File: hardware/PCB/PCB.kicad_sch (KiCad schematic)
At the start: 35 parts, among them J1 USB_C_Receptacle_USB2.0_16P, J2 Conn_01x05_Socket, SW1 SW_Push, SW2 SW_Push, SW3 SW_Push, U1 ESP32-S3-WROOM-1, U2 TPD4E02B04DQA, U3 SX1262 Core, U4 TPS63802DLAR

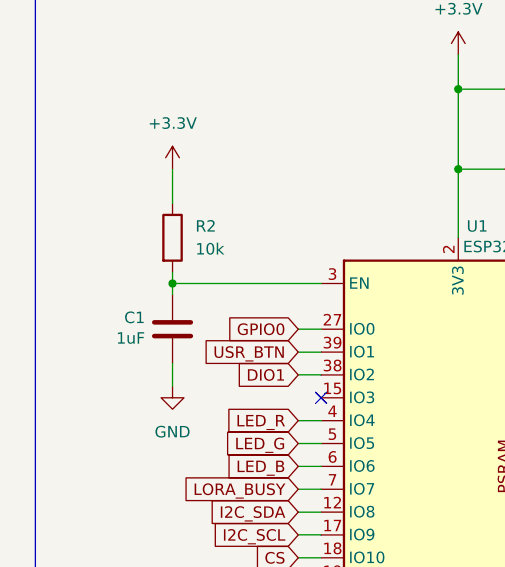
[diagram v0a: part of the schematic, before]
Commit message: feat: més versions de PCB i layouts inicials
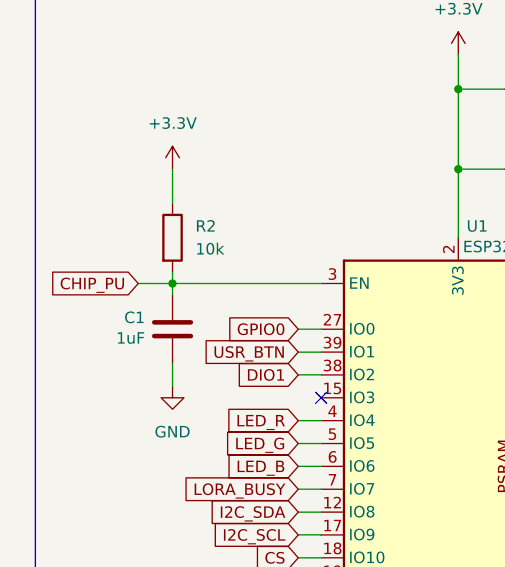
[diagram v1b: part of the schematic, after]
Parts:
- J2: footprint Connector_JST:JST_PH_B5B-PH-K_1x05_P2.00mm_Vertical -> Connector_JST:JST_PH_S5B-PH-K_1x05_P2.00mm_Horizontal
- U4: footprint TPS63802DLAR:VREG_TPS63802DLAR -> TPS63802DLAR_foot:VREG_TPS63802DLAR
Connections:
- net CHIP_PU: now also C1.1, R2.2, U1.3 (EN)
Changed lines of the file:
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@@
 	(wire
 		(pts
+			(xy 25.4 55.88) (xy 29.21 55.88)
+		)
+		(stroke
+			(width 0)
+			(type default)
+		)
+	)
+	(wire
+		(pts
 			(xy 29.21 54.61) (xy 29.21 55.88)
 		)
@@
 		)
 	)
+	(global_label "CHIP_PU"
+		(shape input)
+		(at 25.4 55.88 180)
+		(fields_autoplaced yes)
+		(effects
+			(font
+				(size 1.27 1.27)
+			)
+			(justify right)
+		)
+		(property "Intersheetrefs" "${INTERSHEET_REFS}"
+			(at 14.3714 55.88 0)
+			(effects
+				(font
+					(size 1.27 1.27)
+				)
+				(justify right)
+				(hide yes)
+			)
+		)
+	)
 	(global_label "data-"
 		(shape input)
@@
 			)
 		)
-		(property "Footprint" "Connector_JST:JST_PH_B5B-PH-K_1x05_P2.00mm_Vertical"
+		(property "Footprint" "Connector_JST:JST_PH_S5B-PH-K_1x05_P2.00mm_Horizontal"
 			(at 262.89 118.11 0)
 			(effects
@@
 			)
 		)
-		(property "Footprint" "TPS63802DLAR:VREG_TPS63802DLAR"
+		(property "Footprint" "TPS63802DLAR_foot:VREG_TPS63802DLAR"
 			(at 185.42 69.85 0)
 			(effects
